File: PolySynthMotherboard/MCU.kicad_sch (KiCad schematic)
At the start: 45 parts, among them J201 SWD Header, J202 USB_C_Receptacle_USB2.0, J203 MIDI_In, J204 MIDI_Thru, J205 MIDI_Out, J401 Micro_SD_Card_Det2, SW201 RST, SW202 BOOT, U201 STM32F411RETx, U202 74HC595, U203 74HC595, U204 4N35, U205 74HC04, Y201 16MHz, Y202 32.768kHZ

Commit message: board layout
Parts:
- D201: footprint Diode_THT:D_DO-35_SOD27_P7.62mm_Horizontal -> Diode_SMD:D_SOD-123
- U205: footprint PCM_Package_SO_AKL:SOIC-14_3.9x8.7mm_P1.27mm -> Package_SO:SOIC-14_3.9x8.7mm_P1.27mm
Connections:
- net +3.3V: now also J201.1 (Pin_1); no longer J201.2 (Pin_2)
- net GND: now also J201.3 (Pin_3); no longer J201.1 (Pin_1)
- net NRST: now also J201.5 (Pin_5); no longer J201.6 (Pin_6)
- net SWO: now also J201.6 (Pin_6); no longer J201.5 (Pin_5)
- net TCK: now also J201.2 (Pin_2); no longer J201.3 (Pin_3)
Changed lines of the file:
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@@
     (stroke (width 0) (type default))
   )
+  (wire (pts (xy 115.951 196.342) (xy 115.951 196.723))
+    (stroke (width 0) (type default))
+  )
   (wire (pts (xy 121.158 93.218) (xy 123.698 93.218))
     (stroke (width 0) (type default))
@@
     (stroke (width 0) (type default))
   )
-  (wire (pts (xy 114.554 194.818) (xy 114.554 195.453))
-    (stroke (width 0) (type default))
-  )
   (wire (pts (xy 34.29 109.474) (xy 34.29 121.92))
     (stroke (width 0) (type default))
@@
     (stroke (width 0) (type default))
   )
-  (wire (pts (xy 113.411 197.358) (xy 117.221 197.358))
+  (wire (pts (xy 113.411 194.818) (xy 117.221 194.818))
     (stroke (width 0) (type default))
   )
@@
     (stroke (width 0) (type default))
   )
-  (wire (pts (xy 114.554 195.453) (xy 123.444 195.453))
-    (stroke (width 0) (type default))
-  )
   (wire (pts (xy 81.026 85.598) (xy 85.598 85.598))
     (stroke (width 0) (type default))
@@
     (stroke (width 0) (type default))
   )
+  (wire (pts (xy 113.411 196.342) (xy 115.951 196.342))
+    (stroke (width 0) (type default))
+  )
   (wire (pts (xy 121.158 65.278) (xy 156.718 65.278))
     (stroke (width 0) (type default))
@@
     (stroke (width 0) (type default))
   )
-  (wire (pts (xy 113.411 194.818) (xy 114.554 194.818))
-    (stroke (width 0) (type default))
-  )
   (wire (pts (xy 200.914 81.026) (xy 204.724 81.026))
     (stroke (width 0) (type default))
@@
     (stroke (width 0) (type default))
   )
-  (wire (pts (xy 123.444 195.453) (xy 123.444 193.167))
-    (stroke (width 0) (type default))
-  )
   (wire (pts (xy 200.406 134.874) (xy 203.454 134.874))
     (stroke (width 0) (type default))
@@
     (stroke (width 0) (type default))
   )
+  (wire (pts (xy 113.411 197.358) (xy 113.411 196.342))
+    (stroke (width 0) (type default))
+  )
   (wire (pts (xy 83.566 113.538) (xy 85.598 113.538))
     (stroke (width 0) (type default))
@@
     (stroke (width 0) (type default))
   )
-  (wire (pts (xy 113.411 204.978) (xy 117.221 204.978))
+  (wire (pts (xy 113.411 202.438) (xy 117.221 202.438))
     (stroke (width 0) (type default))
   )
@@
     (stroke (width 0) (type default))
   )
+  (wire (pts (xy 113.411 192.278) (xy 117.983 192.278))
+    (stroke (width 0) (type default))
+  )
   (wire (pts (xy 46.482 54.356) (xy 46.482 57.15))
     (stroke (width 0) (type default))
@@
     (stroke (width 0) (type default))
   )
-  (wire (pts (xy 113.411 202.438) (xy 117.221 202.438))
+  (wire (pts (xy 113.411 204.978) (xy 117.221 204.978))
     (stroke (width 0) (type default))
   )
@@
     (stroke (width 0) (type default))
   )
+  (wire (pts (xy 117.983 192.278) (xy 117.983 192.151))
+    (stroke (width 0) (type default))
+  )
   (wire (pts (xy 76.454 201.168) (xy 76.454 202.946))
     (stroke (width 0) (type default))
@@
     (stroke (width 0) (type default))
   )
-  (wire (pts (xy 113.411 192.278) (xy 118.364 192.278))
-    (stroke (width 0) (type default))
-  )
   (wire (pts (xy 279.654 50.419) (xy 286.639 50.419))
     (stroke (width 0) (type default))
@@
     )
   )
-  (global_label "SWO" (shape input) (at 117.221 202.438 0) (fields_autoplaced)
+  (global_label "SWO" (shape input) (at 117.221 204.978 0) (fields_autoplaced)
     (effects (font (size 1.27 1.27)) (justify left))
-    (property "Intersheetrefs" "${INTERSHEET_REFS}" (at 124.1976 202.438 0)
+    (property "Intersheetrefs" "${INTERSHEET_REFS}" (at 124.1976 204.978 0)
       (effects (font (size 1.27 1.27)) (justify left) hide)
     )
@@
     )
   )
-  (global_label "TCK" (shape input) (at 117.221 197.358 0) (fields_autoplaced)
+  (global_label "TCK" (shape input) (at 117.221 194.818 0) (fields_autoplaced)
     (effects (font (size 1.27 1.27)) (justify left))
-    (property "Intersheetrefs" "${INTERSHEET_REFS}" (at 123.7138 197.358 0)
+    (property "Intersheetrefs" "${INTERSHEET_REFS}" (at 123.7138 194.818 0)
       (effects (font (size 1.27 1.27)) (justify left) hide)
     )
@@
     )
   )
-  (global_label "NRST" (shape input) (at 117.221 204.978 0) (fields_autoplaced)
+  (global_label "NRST" (shape input) (at 117.221 202.438 0) (fields_autoplaced)
     (effects (font (size 1.27 1.27)) (justify left))
-    (property "Intersheetrefs" "${INTERSHEET_REFS}" (at 124.9838 204.978 0)
+    (property "Intersheetrefs" "${INTERSHEET_REFS}" (at 124.9838 202.438 0)
       (effects (font (size 1.27 1.27)) (justify left) hide)
     )
@@
       (effects (font (size 1.27 1.27)))
     )
-    (property "Footprint" "PCM_Package_SO_AKL:SOIC-14_3.9x8.7mm_P1.27mm" (at 345.059 149.987 0)
+    (property "Footprint" "Package_SO:SOIC-14_3.9x8.7mm_P1.27mm" (at 345.059 149.987 0)
       (effects (font (size 1.27 1.27)) hide)
     )
@@
       (effects (font (size 1.27 1.27)) (justify right))
     )
-    (property "Footprint" "Diode_THT:D_DO-35_SOD27_P7.62mm_Horizontal" (at 353.695 52.705 0)
+    (property "Footprint" "Diode_SMD:D_SOD-123" (at 353.695 52.705 0)
       (effects (font (size 1.27 1.27)) hide)
     )
@@
       (effects (font (size 1.27 1.27)))
     )
-    (property "Footprint" "PCM_Package_SO_AKL:SOIC-14_3.9x8.7mm_P1.27mm" (at 347.091 84.074 0)
+    (property "Footprint" "Package_SO:SOIC-14_3.9x8.7mm_P1.27mm" (at 347.091 84.074 0)
       (effects (font (size 1.27 1.27)) hide)
     )
@@
       (effects (font (size 1.27 1.27)))
     )
-    (property "Footprint" "PCM_Package_SO_AKL:SOIC-14_3.9x8.7mm_P1.27mm" (at 363.347 84.074 0)
+    (property "Footprint" "Package_SO:SOIC-14_3.9x8.7mm_P1.27mm" (at 363.347 84.074 0)
       (effects (font (size 1.27 1.27)) hide)
     )
@@
       (effects (font (size 1.27 1.27)) (justify left))
     )
-    (property "Footprint" "PCM_Package_SO_AKL:SOIC-14_3.9x8.7mm_P1.27mm" (at 387.731 151.511 0)
+    (property "Footprint" "Package_SO:SOIC-14_3.9x8.7mm_P1.27mm" (at 387.731 151.511 0)
       (effects (font (size 1.27 1.27)) hide)
     )
@@
       (effects (font (size 1.27 1.27)))
     )
-    (property "Footprint" "PCM_Package_SO_AKL:SOIC-14_3.9x8.7mm_P1.27mm" (at 361.696 149.987 0)
+    (property "Footprint" "Package_SO:SOIC-14_3.9x8.7mm_P1.27mm" (at 361.696 149.987 0)
       (effects (font (size 1.27 1.27)) hide)
     )
@@
     )
   )
-  (symbol (lib_id "power:GND") (at 118.364 192.278 0) (unit 1)
+  (symbol (lib_id "power:GND") (at 115.951 196.723 0) (unit 1)
     (in_bom yes) (on_board yes) (dnp no) (fields_autoplaced)
-    (property "Reference" "#PWR0239" (at 118.364 198.628 0)
+    (property "Reference" "#PWR0239" (at 115.951 203.073 0)
       (effects (font (size 1.27 1.27)) hide)
     )
-    (property "Value" "GND" (at 118.364 196.088 0)
+    (property "Value" "GND" (at 115.951 200.533 0)
       (effects (font (size 1.27 1.27)) hide)
     )
-    (property "Footprint" "" (at 118.364 192.278 0)
+    (property "Footprint" "" (at 115.951 196.723 0)
       (effects (font (size 1.27 1.27)) hide)
     )
-    (property "Datasheet" "" (at 118.364 192.278 0)
+    (property "Datasheet" "" (at 115.951 196.723 0)
       (effects (font (size 1.27 1.27)) hide)
     )
@@
     )
   )
-  (symbol (lib_id "power:+3.3V") (at 123.444 193.167 0) (unit 1)
+  (symbol (lib_id "power:+3.3V") (at 117.983 192.151 0) (unit 1)
     (in_bom yes) (on_board yes) (dnp no) (fields_autoplaced)
-    (property "Reference" "#PWR0240" (at 123.444 196.977 0)
+    (property "Reference" "#PWR0240" (at 117.983 195.961 0)
       (effects (font (size 1.27 1.27)) hide)
     )
-    (property "Value" "+3.3V" (at 123.444 188.214 0)
+    (property "Value" "+3.3V" (at 117.983 187.198 0)
       (effects (font (size 1.27 1.27)))
     )
-    (property "Footprint" "" (at 123.444 193.167 0)
+    (property "Footprint" "" (at 117.983 192.151 0)
       (effects (font (size 1.27 1.27)) hide)
     )
-    (property "Datasheet" "" (at 123.444 193.167 0)
+    (property "Datasheet" "" (at 117.983 192.151 0)
       (effects (font (size 1.27 1.27)) hide)
     )
@@
       (effects (font (size 1.27 1.27)))
     )
-    (property "Footprint" "PCM_Package_SO_AKL:SOIC-14_3.9x8.7mm_P1.27mm" (at 364.871 113.792 0)
+    (property "Footprint" "Package_SO:SOIC-14_3.9x8.7mm_P1.27mm" (at 364.871 113.792 0)
       (effects (font (size 1.27 1.27)) hide)
     )
@@
       (effects (font (size 1.27 1.27)))
     )
-    (property "Footprint" "PCM_Package_SO_AKL:SOIC-14_3.9x8.7mm_P1.27mm" (at 346.71 113.792 0)
+    (property "Footprint" "Package_SO:SOIC-14_3.9x8.7mm_P1.27mm" (at 346.71 113.792 0)
       (effects (font (size 1.27 1.27)) hide)
     )

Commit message: new voice board proj
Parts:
- J202: value USB_C_Receptacle_USB2.0 -> USB_C_Leceptacle_USB2.0
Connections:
- net BATT_REF renamed BATT_LEF
- net DISP_RST renamed DISP_LST
- net MIDI_RX renamed MIDI_LX
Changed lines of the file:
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@@
     )
   )
-  (global_label "MIDI_RX" (shape input) (at 124.206 108.458 0) (fields_autoplaced)
+  (global_label "MIDI_LX" (shape input) (at 124.206 108.458 0) (fields_autoplaced)
     (effects (font (size 1.27 1.27)) (justify left))
     (property "Intersheetrefs" "${INTERSHEET_REFS}" (at 134.5693 108.458 0)
@@
     )
   )
-  (global_label "MIDI_RX" (shape output) (at 384.937 47.244 0) (fields_autoplaced)
+  (global_label "MIDI_LX" (shape output) (at 384.937 47.244 0) (fields_autoplaced)
     (effects (font (size 1.27 1.27)) (justify left))
     (property "Intersheetrefs" "${INTERSHEET_REFS}" (at 395.3003 47.244 0)
@@
     )
   )
-  (global_label "BATT_REF" (shape input) (at 81.788 72.898 180) (fields_autoplaced)
+  (global_label "BATT_LEF" (shape input) (at 81.788 72.898 180) (fields_autoplaced)
     (effects (font (size 1.27 1.27)) (justify right))
     (property "Intersheetrefs" "${INTERSHEET_REFS}" (at 70.0338 72.898 0)
@@
     )
   )
-  (global_label "DISP_RST" (shape output) (at 124.206 103.378 0) (fields_autoplaced)
+  (global_label "DISP_LST" (shape output) (at 124.206 103.378 0) (fields_autoplaced)
     (effects (font (size 1.27 1.27)) (justify left))
     (property "Intersheetrefs" "${INTERSHEET_REFS}" (at 135.9602 103.378 0)
@@
       (effects (font (size 1.27 1.27)))
     )
-    (property "Value" "USB_C_Receptacle_USB2.0" (at 170.688 177.8 0)
-      (effects (font (size 1.27 1.27)))
-    )
+    (property "Value" "USB_C_Leceptacle_USB2.0" (at 170.688 177.8 0)
+      (effects (font (size 1.27 1.27)))
+    )

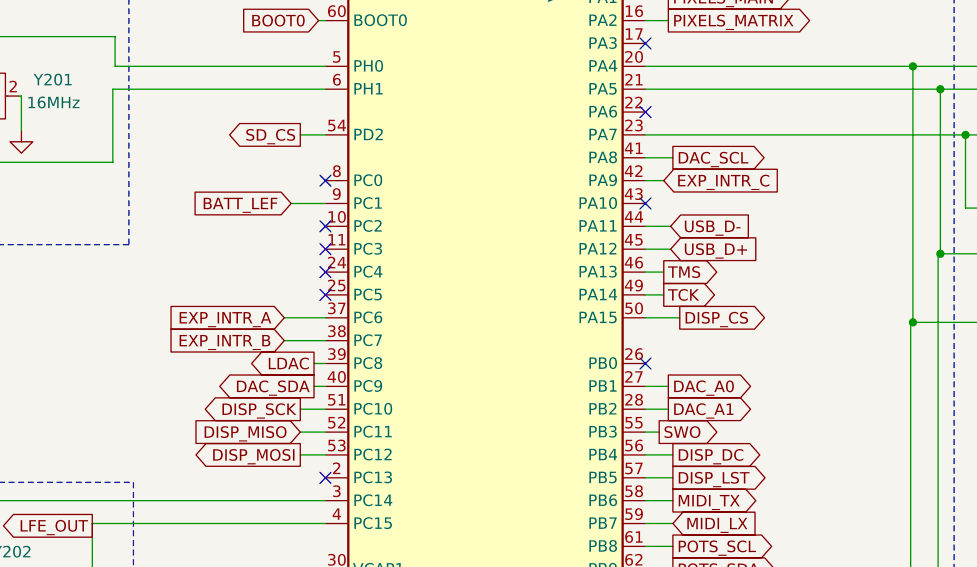
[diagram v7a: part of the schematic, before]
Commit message: op-amp layout improved
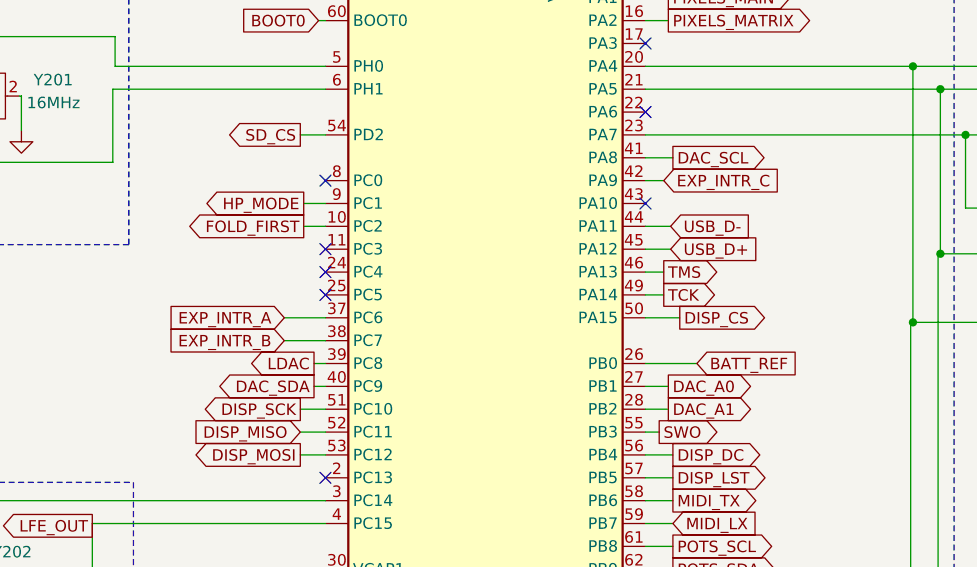
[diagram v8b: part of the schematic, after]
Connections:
- net FOLD_FIRST: now reaches U201.10 (PC2)
- net BATT_REF: now reaches U201.26 (PB0)
- net BATT_LEF renamed HP_MODE
- no-connect marks 27 -> 25
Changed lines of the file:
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@@
   (no_connect (at 354.076 149.987))
   (no_connect (at 369.316 149.987))
-  (no_connect (at 121.158 90.678))
   (no_connect (at 279.654 47.879))
   (no_connect (at 200.406 142.494))
   (no_connect (at 352.679 149.987))
   (no_connect (at 200.406 150.114))
-  (no_connect (at 85.598 75.438))
   (no_connect (at 85.598 83.058))
   (no_connect (at 372.999 44.704))
@@
     (stroke (width 0) (type default))
   )
+  (wire (pts (xy 121.158 90.678) (xy 126.873 90.678))
+    (stroke (width 0) (type default))
+  )
   (wire (pts (xy 308.102 48.387) (xy 308.102 50.927))
     (stroke (width 0) (type default))
@@
     (stroke (width 0) (type default))
   )
+  (wire (pts (xy 83.185 72.898) (xy 85.598 72.898))
+    (stroke (width 0) (type default))
+  )
   (wire (pts (xy 83.566 123.19) (xy 83.566 124.46))
     (stroke (width 0) (type default))
@@
     (stroke (width 0) (type default))
   )
-  (wire (pts (xy 81.788 72.898) (xy 85.598 72.898))
-    (stroke (width 0) (type default))
-  )
   (wire (pts (xy 156.718 65.278) (xy 158.496 65.278))
     (stroke (width 0) (type default))
@@
   )
   (wire (pts (xy 339.471 84.074) (xy 334.137 84.074))
+    (stroke (width 0) (type default))
+  )
+  (wire (pts (xy 83.185 75.438) (xy 85.598 75.438))
     (stroke (width 0) (type default))
   )
@@
     )
   )
+  (global_label "FOLD_FIRST" (shape output) (at 83.185 75.438 180) (fields_autoplaced)
+    (effects (font (size 1.27 1.27)) (justify right))
+    (property "Intersheetrefs" "${INTERSHEET_REFS}" (at 69.3745 75.438 0)
+      (effects (font (size 1.27 1.27)) (justify right) hide)
+    )
+  )
   (global_label "EXP_SCK" (shape output) (at 123.698 121.158 0) (fields_autoplaced)
     (effects (font (size 1.27 1.27)) (justify left))
@@
     )
   )
+  (global_label "HP_MODE" (shape output) (at 83.185 72.898 180) (fields_autoplaced)
+    (effects (font (size 1.27 1.27)) (justify right))
+    (property "Intersheetrefs" "${INTERSHEET_REFS}" (at 71.4308 72.898 0)
+      (effects (font (size 1.27 1.27)) (justify right) hide)
+    )
+  )
   (global_label "PIXELS_MAIN" (shape output) (at 123.698 50.038 0) (fields_autoplaced)
     (effects (font (size 1.27 1.27)) (justify left))
@@
     )
   )
-  (global_label "BATT_LEF" (shape input) (at 81.788 72.898 180) (fields_autoplaced)
-    (effects (font (size 1.27 1.27)) (justify right))
-    (property "Intersheetrefs" "${INTERSHEET_REFS}" (at 70.0338 72.898 0)
-      (effects (font (size 1.27 1.27)) (justify right) hide)
-    )
-  )
+  (global_label "BATT_REF" (shape input) (at 126.873 90.678 0) (fields_autoplaced)
+    (effects (font (size 1.27 1.27)) (justify left))
+    (property "Intersheetrefs" "${INTERSHEET_REFS}" (at 138.6272 90.678 0)
+      (effects (font (size 1.27 1.27)) (justify left) hide)
+    )
+  )
